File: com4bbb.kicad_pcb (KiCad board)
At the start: 4 copper layers, 54.6 x 86.4 mm, 66 parts, among them J101 RS485, J102 PWR, J103 DCF77, J201 USB_B_Micro, J202 JTAG, P8 BeagleBone_Black_Header, P9 BeagleBone_Black_Header, SW101 Reset, SW102 PWR, U101 SP3485EN, U102 R-78K5.0-0.5, U103 AT24C512C-SSHD-T, U104 ATECC608A-MAHDA, U105 DS3231MZ, U201 USBLC6-2SC6, U202 ESP32-S3-WROOM-1

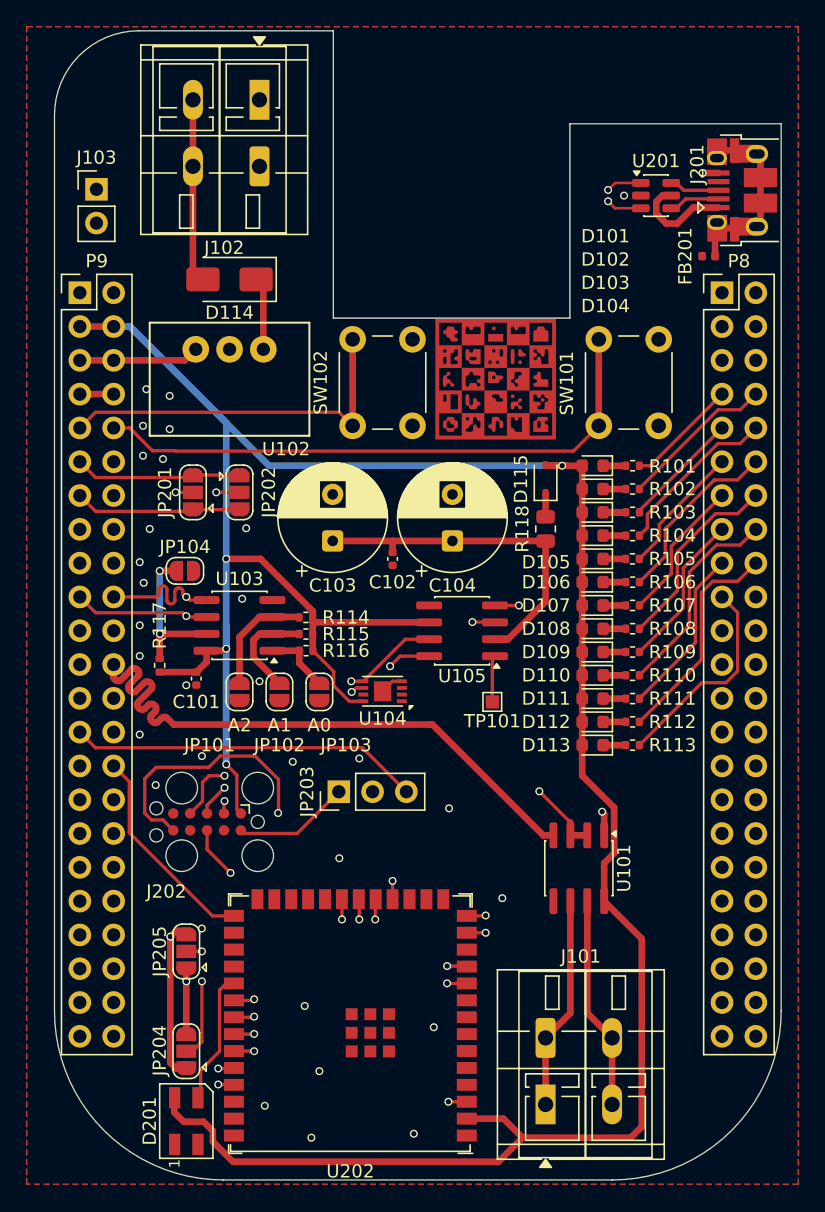
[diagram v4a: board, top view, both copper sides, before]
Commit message: Add PPS input
Signed-off-by: Benedikt Spranger <b.spranger@linutronix.de>
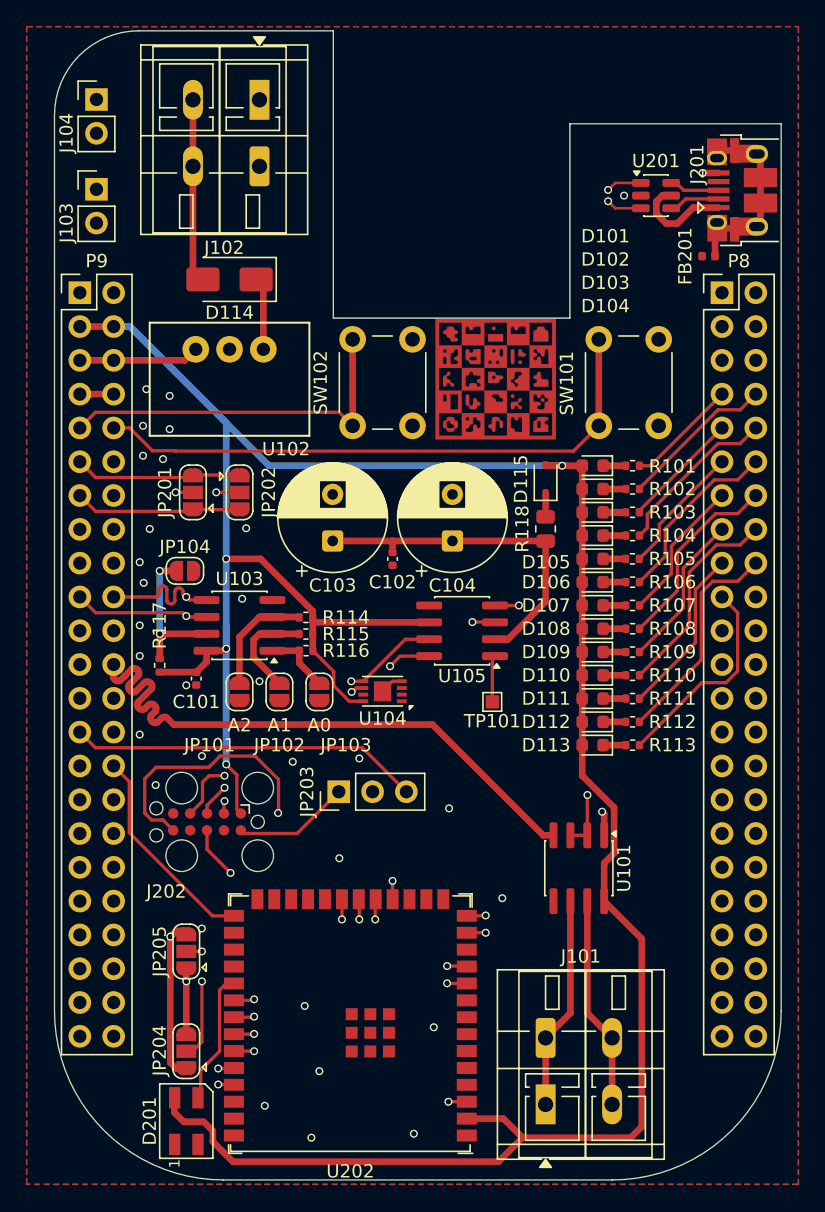
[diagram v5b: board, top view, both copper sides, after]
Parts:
- added J104: PPS, Connector_PinHeader_2.54mm:PinHeader_1x02_P2.54mm_Vertical, F.Cu at (117.6, 47.9)
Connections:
- P8 pad 26: unconnected-(P8-Pin_26-Pad26) -> /DE/~{RE}
- P9 pad 15: /GPIO_48 -> /PPS
- U101 pad 2: /GPIO_48 -> /DE/~{RE}
- U101 pad 3: /GPIO_48 -> /DE/~{RE}
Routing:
- net /GPIO_48: track 49.2 -> 0.00 mm, vias 1 -> 0
- net /PPS: track 0.00 -> 33.7 mm
- net /DE/~{RE}: track 0.00 -> 20.0 mm, vias 0 -> 1
- net Net-(D201-DIN): track 10.1 -> 9.18 mm
- net /GPIO_60: track 54.8 -> 54.1 mm
- net Net-(JP204-C): track 22.5 -> 22.0 mm
